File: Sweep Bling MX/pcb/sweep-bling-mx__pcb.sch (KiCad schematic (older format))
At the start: 46 parts, among them J1 AudioJack4dpb, J2 AudioJack4dpb, SW10 SW_Push, SW10_r1 SW_Push, SW11 SW_Push, SW11_r1 SW_Push, SW12 SW_Push, SW12_r1 SW_Push, SW13_r1 SW_Push, SW14 SW_Push, SW14_r1 SW_Push, SW15 SW_Push, SW15_r1 SW_Push, SW16 SW_Push, SW16_r1 SW_Push, SW17 SW_Push, SW17_r1 SW_Push, SW18 SW_Push, SW18_r1 SW_Push, SW2 SW_Push, SW20 SW_Push, SW21 SW_Push, SW2_r1 SW_Push, SW3 SW_Push, SW3_r1 SW_Push, SW4 SW_Push, SW4_r1 SW_Push, SW5 SW_Push, SW5_r1 SW_Push, SW6 SW_Push, SW6_r1 SW_Push, SW7_r1 SW_Push, SW8 SW_Push, SW8_r1 SW_Push, SW9 SW_Push, SW9_r1 SW_Push, U1 ProMicro-kbd, U2 ProMicro-kbd

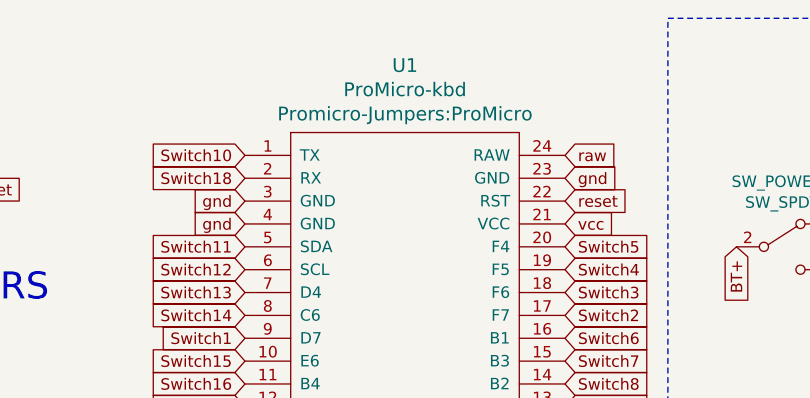
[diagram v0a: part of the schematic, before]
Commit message: Update silk and MCU orientation
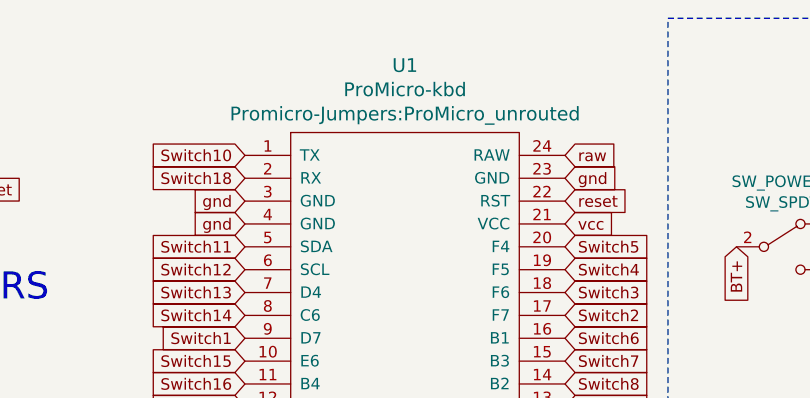
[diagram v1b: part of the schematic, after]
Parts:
- U1: footprint Promicro-Jumpers:ProMicro -> Promicro-Jumpers:ProMicro_unrouted
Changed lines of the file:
@@
 F 0 "U1" H 6950 3293 60  0000 C CNN
 F 1 "ProMicro-kbd" H 6950 3187 60  0000 C CNN
-F 2 "Promicro-Jumpers:ProMicro" H 6950 3081 60  0000 C CNN
+F 2 "Promicro-Jumpers:ProMicro_unrouted" H 6950 3081 60  0000 C CNN
 F 3 "" H 7050 1100 60  0000 C CNN
 	1    6950 2150
